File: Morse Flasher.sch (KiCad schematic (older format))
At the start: 7 parts, among them U1 ATTINY25-45-85/DIP-SO

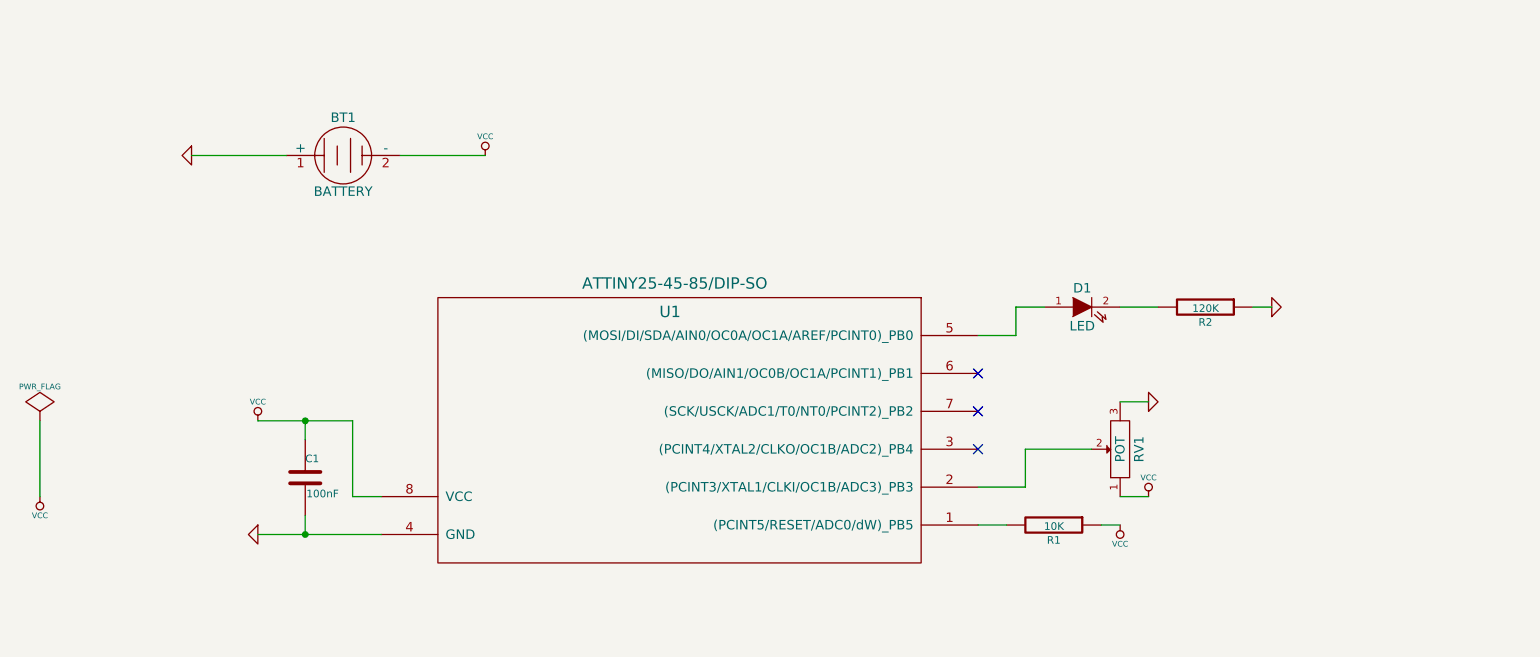
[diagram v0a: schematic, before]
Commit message: Version sent to OSHPark
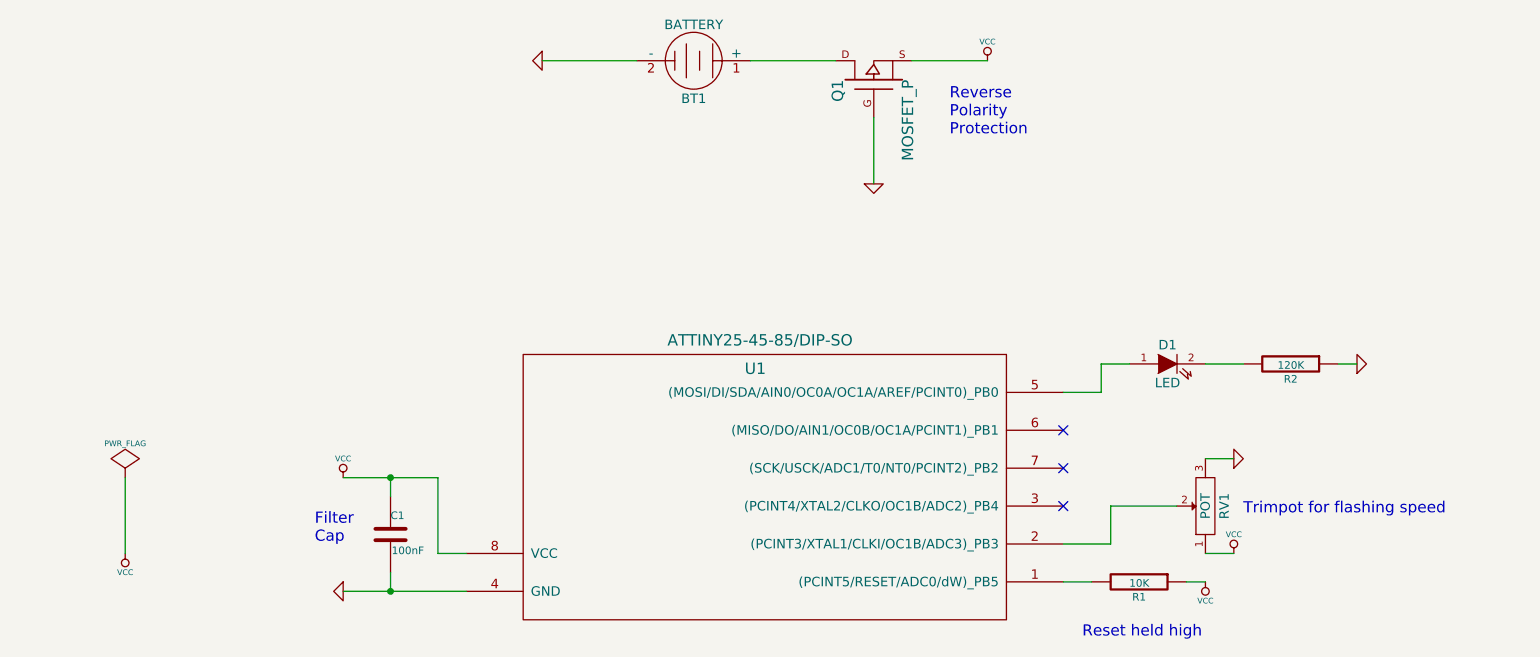
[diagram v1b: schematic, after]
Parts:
- added Q1: MOSFET_P, symbol MOSFET_P
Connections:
- net GND: now also BT1.2 (-), Q1.G; no longer BT1.1 (+)
- net VCC: now also Q1.S; no longer BT1.2 (-)
- new net: BT1.1 (+), Q1.D
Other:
- note added: "Filter\nCap"
- note added: "Reset held high"
- note added: "Reverse \nPolarity \nProtection"
- note added: "Trimpot for flashing speed"
- moved on the sheet: BT1, C1, D1, R1, R2, RV1, U1
